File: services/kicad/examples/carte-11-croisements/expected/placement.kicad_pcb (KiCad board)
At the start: 2 copper layers, 140 x 120 mm, 6 parts, among them J1 BUS_A, J2 BUS_B

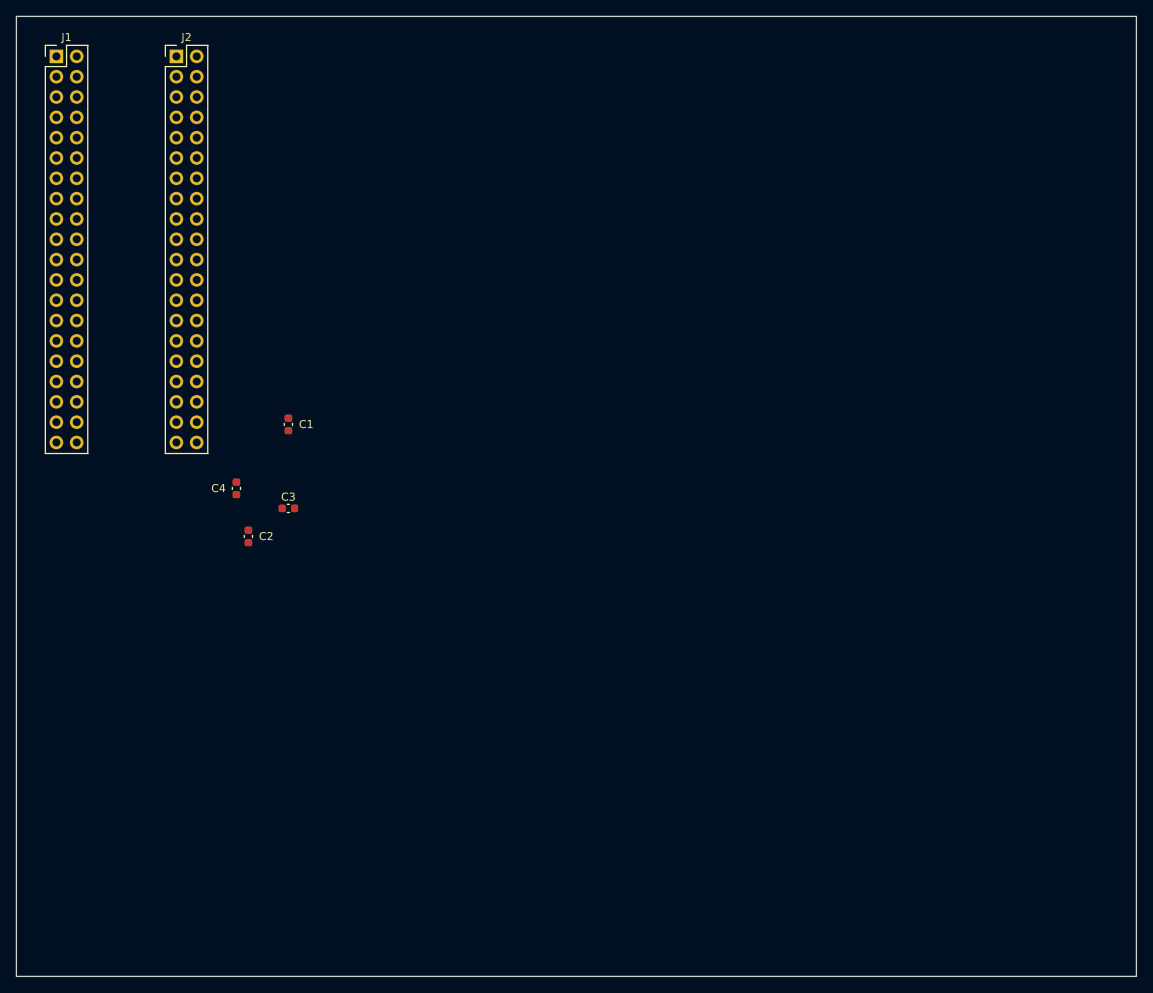
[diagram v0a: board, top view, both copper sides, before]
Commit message: banc(rejeu): douze cartes hors le banc des dix, et le trou qu elles ont revele
Demande : refaire placement et routage de toutes les cartes d `examples/`
SAUF les dix du banc, sans toucher `stm32-validation` ni `STM32-Test`.

DOUZE CARTES REJOUEES, DEUX FAMILLES.

  groupe A (input/schema.json)        regenerer_le_banc.py — garde le meilleur
      carte-11-croisements            100 % · 0 err · 0 perdu   GARDE
      driver-clignotant-ne555         100 % · 0 err · 0 perdu   GARDE
      driver-stm32-minimal            100 % · 0 err · 0 perdu   GARDE
      driver-thermometre-i2c          100 % · 0 err · 0 perdu   GARDE

  groupe B (input/circuit.json)       banc_exemples.py — ecrit dans output/
      arduino-uno       2 couches  100 %  0 manq  0 err    925 s
      esp32-baseline    2 couches  100 %  0 manq  0 err    387 s
      led-blinker       2 couches  100 %  0 manq  0 err    124 s
      nucleo-f401       4 couches   98 %  1 manq  0 err   1814 s
      stm32-baseline    2 couches  100 %  0 manq  0 err    193 s
      stm32-30          2 couches  100 %  0 manq  0 err    404 s
      stm32-60          2 couches  100 %  0 manq  0 err    414 s
      stm32-100         2 couches  100 %  0 manq  0 err    308 s

LE REJEU CONFIRME LES BOARDS LIVRES — ON NE REMPLACE RIEN.

DRC des boards VERSIONNES face aux boards du rejeu, meme instrument
(`kicad-cli pcb drc --severity-all`) des deux cotes :

      sept cartes            0 err · 0 manq des DEUX cotes   egalite
      nucleo-f401            0 manq versionne, 1 au rejeu    on garde l ancien

Livrer des boards de qualite identique ferait du bruit sans rien apporter, et
le tirage de `nucleo-f401` est moins bon : la protection a joue exactement
comme prevu.

LE TROU : CES HUIT CARTES N AVAIENT AUCUN `mesures.json`.

Leur board etait livre depuis le 2026-09-07 et RIEN ne disait ce qu il valait.
Un lecteur ne pouvait ni le verifier ni s en apercevoir — c est la faute que ce
depot poursuit partout, appliquee non pas a un compteur mais a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
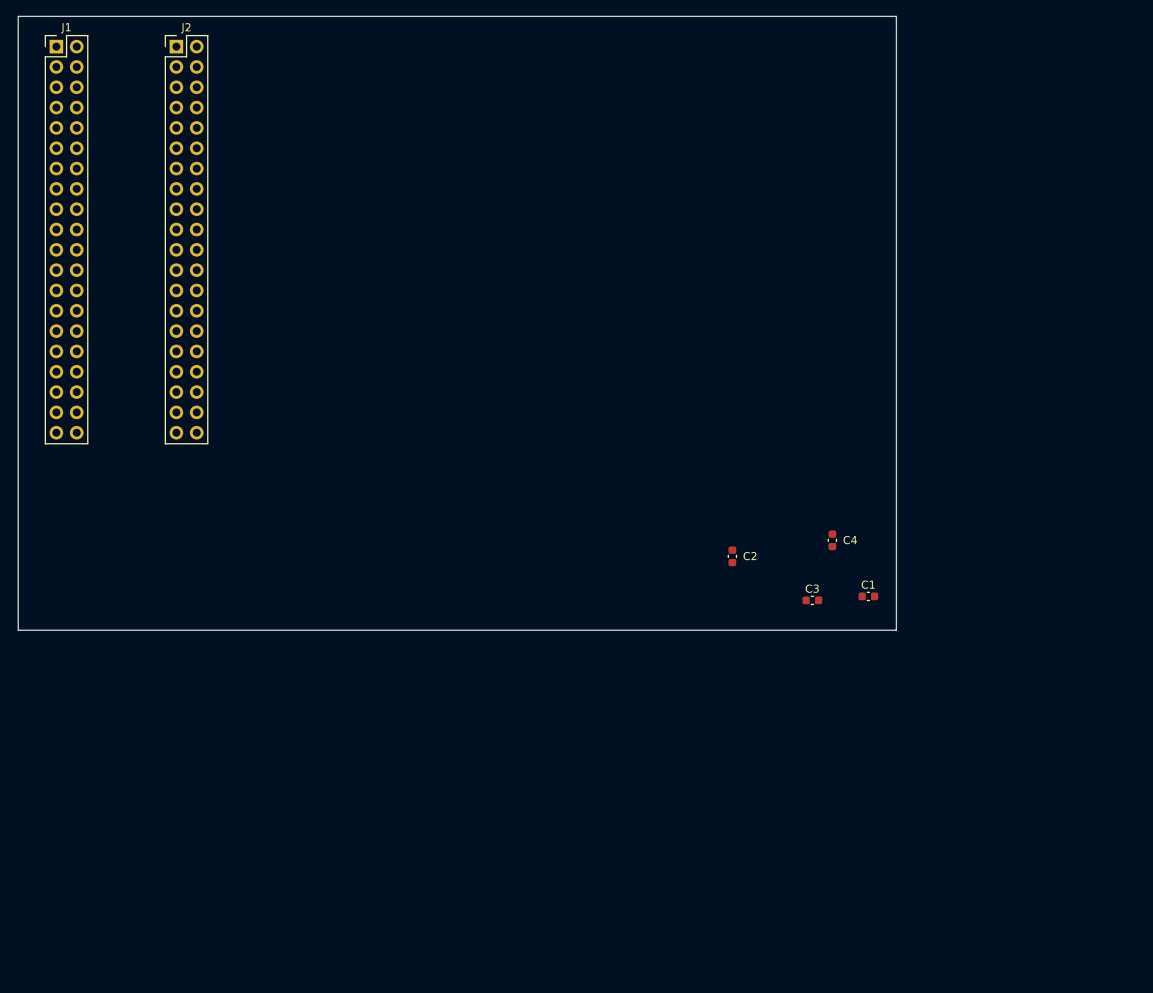
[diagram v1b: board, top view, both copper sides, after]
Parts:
- moved C1 75.6 mm to (185.0, 117.5), turned to 0 degrees
- moved C4 74.8 mm to (180.5, 110.5), turned to 270 degrees
- moved C3 66.5 mm to (178.0, 118.0)
- moved C2 60.6 mm to (168.0, 112.5)
- moved J1 1.22 mm to (83.5, 48.8)
- moved J2 1.22 mm to (98.5, 48.8)
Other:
- board size 140 x 120 mm -> 109.8 x 76.7 mm
